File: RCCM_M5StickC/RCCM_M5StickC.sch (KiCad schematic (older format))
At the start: 7 parts, among them CN1 Conn_02x04_Odd_Even, CN2 Conn_01x04, CN3 Conn_01x04, CN4 Conn_01x08

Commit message: Gerber change
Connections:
- net G33: now also S3.6 (Pin_6); no longer S1.6 (Pin_6)
- net SD0: now also S1.6 (Pin_6); no longer S3.6 (Pin_6)
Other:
- moved on the sheet: S1, S3
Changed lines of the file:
@@
 L Conn_01x06 S1
 U 1 1 5EB9082C
-P 1200 1150
-F 0 "S1" H 1200 1450 50  0000 C CNN
-F 1 "Conn_01x06" H 1200 750 50  0000 C CNN
-F 2 "Pin_Headers:Pin_Header_Straight_1x06_Pitch2.54mm" H 1200 1150 50  0001 C CNN
-F 3 "" H 1200 1150 50  0001 C CNN
-	1    1200 1150
+P 2950 1150
+F 0 "S1" H 2950 1450 50  0000 C CNN
+F 1 "Conn_01x06" H 2950 750 50  0000 C CNN
+F 2 "Pin_Headers:Pin_Header_Straight_1x06_Pitch2.54mm" H 2950 1150 50  0001 C CNN
+F 3 "" H 2950 1150 50  0001 C CNN
+	1    2950 1150
 	0    1    -1   0
 $EndComp
@@
 L Conn_01x06 S3
 U 1 1 5EB908B2
-P 2950 1150
-F 0 "S3" H 2950 1450 50  0000 C CNN
-F 1 "Conn_01x06" H 2950 750 50  0000 C CNN
-F 2 "Pin_Headers:Pin_Header_Straight_1x06_Pitch2.54mm" H 2950 1150 50  0001 C CNN
-F 3 "" H 2950 1150 50  0001 C CNN
-	1    2950 1150
+P 1200 1150
+F 0 "S3" H 1200 1450 50  0000 C CNN
+F 1 "Conn_01x06" H 1200 750 50  0000 C CNN
+F 2 "Pin_Headers:Pin_Header_Straight_1x06_Pitch2.54mm" H 1200 1150 50  0001 C CNN
+F 3 "" H 1200 1150 50  0001 C CNN
+	1    1200 1150
 	0    1    -1   0
 $EndComp

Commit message: Gerber Update
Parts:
- added R1, R2: R, Resistors_THT:R_Axial_DIN0207_L6.3mm_D2.5mm_P2.54mm_Vertical, symbol R
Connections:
- net 3V3m: now also R1.1, R2.1
- net G00: now also CN1.8 (Pin_8), CN3.3 (Pin_3), S1.4 (Pin_4), S2.4 (Pin_4), S3.4 (Pin_4), R1.2; no longer CN1.6 (Pin_6), CN3.4 (Pin_4), S1.3 (Pin_3), S2.3 (Pin_3), S3.3 (Pin_3)
- net G26: now also CN1.6 (Pin_6), CN3.4 (Pin_4), S1.3 (Pin_3), S2.3 (Pin_3), S3.3 (Pin_3), R2.2; no longer CN1.8 (Pin_8), CN3.3 (Pin_3), S1.4 (Pin_4), S2.4 (Pin_4), S3.4 (Pin_4)
- net G33: now also S1.6 (Pin_6); no longer S3.6 (Pin_6)
- net SD0: now also S3.6 (Pin_6); no longer S1.6 (Pin_6)
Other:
- moved on the sheet: S1, S3
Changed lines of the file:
@@
 L Conn_01x06 S1
 U 1 1 5EB9082C
-P 2950 1150
-F 0 "S1" H 2950 1450 50  0000 C CNN
-F 1 "Conn_01x06" H 2950 750 50  0000 C CNN
-F 2 "Pin_Headers:Pin_Header_Straight_1x06_Pitch2.54mm" H 2950 1150 50  0001 C CNN
-F 3 "" H 2950 1150 50  0001 C CNN
-	1    2950 1150
+P 1200 1150
+F 0 "S1" H 1200 1450 50  0000 C CNN
+F 1 "Conn_01x06" H 1200 750 50  0000 C CNN
+F 2 "Pin_Headers:Pin_Header_Straight_1x06_Pitch2.54mm" H 1200 1150 50  0001 C CNN
+F 3 "" H 1200 1150 50  0001 C CNN
+	1    1200 1150
 	0    1    -1   0
 $EndComp
@@
 L Conn_01x06 S3
 U 1 1 5EB908B2
-P 1200 1150
-F 0 "S3" H 1200 1450 50  0000 C CNN
-F 1 "Conn_01x06" H 1200 750 50  0000 C CNN
-F 2 "Pin_Headers:Pin_Header_Straight_1x06_Pitch2.54mm" H 1200 1150 50  0001 C CNN
-F 3 "" H 1200 1150 50  0001 C CNN
-	1    1200 1150
+P 2950 1150
+F 0 "S3" H 2950 1450 50  0000 C CNN
+F 1 "Conn_01x06" H 2950 750 50  0000 C CNN
+F 2 "Pin_Headers:Pin_Header_Straight_1x06_Pitch2.54mm" H 2950 1150 50  0001 C CNN
+F 3 "" H 2950 1150 50  0001 C CNN
+	1    2950 1150
 	0    1    -1   0
 $EndComp
@@
 Text Notes 700  850  0    118  ~ 0
 Sensor
-Text GLabel 4900 2050 2    60   Input ~ 0
-G26
-Text GLabel 4900 2150 2    60   Input ~ 0
-G00
 Text GLabel 4650 3850 2    60   Input ~ 0
 G32
@@
 Text GLabel 4450 3950 0    60   Input ~ 0
 SD2
+Text GLabel 4650 3600 2    60   Input ~ 0
+G26
 Text GLabel 4650 3500 2    60   Input ~ 0
-G26
-Text GLabel 4650 3600 2    60   Input ~ 0
 G00
 Text GLabel 4450 3350 0    60   Input ~ 0
@@
 	1100 1800 1100 1350
 Connection ~ 2000 1800
+$Comp
+L R R1
+U 1 1 5EC75A3F
+P 5200 2650
+F 0 "R1" V 5280 2650 50  0000 C CNN
+F 1 "R" V 5200 2650 50  0000 C CNN
+F 2 "Resistors_THT:R_Axial_DIN0207_L6.3mm_D2.5mm_P2.54mm_Vertical" V 5130 2650 50  0001 C CNN
+F 3 "" H 5200 2650 50  0001 C CNN
+	1    5200 2650
+	1    0    0    -1
+$EndComp
+Text GLabel 4900 2050 2    60   Input ~ 0
+SDA
+Text GLabel 4900 2150 2    60   Input ~ 0
+SCL
+Text GLabel 4650 2450 0    60   Input ~ 0
+3V3m
+Text GLabel 4650 2850 0    60   Input ~ 0
+SDA
+Text GLabel 4650 2950 0    60   Input ~ 0
+SCL
+Wire Wire Line
+	4650 2450 5400 2450
+Wire Wire Line
+	5200 2450 5200 2500
+Wire Wire Line
+	4650 2850 5200 2850
+Wire Wire Line
+	5200 2850 5200 2800
+$Comp
+L R R2
+U 1 1 5EC75CCF
+P 5400 2650
+F 0 "R2" V 5480 2650 50  0000 C CNN
+F 1 "R" V 5400 2650 50  0000 C CNN
+F 2 "Resistors_THT:R_Axial_DIN0207_L6.3mm_D2.5mm_P2.54mm_Vertical" V 5330 2650 50  0001 C CNN
+F 3 "" H 5400 2650 50  0001 C CNN
+	1    5400 2650
+	1    0    0    -1
+$EndComp
+Wire Wire Line
+	5400 2450 5400 2500
+Connection ~ 5200 2450
+Wire Wire Line
+	5400 2800 5400 2950
+Wire Wire Line
+	5400 2950 4650 2950
 $EndSCHEMATC

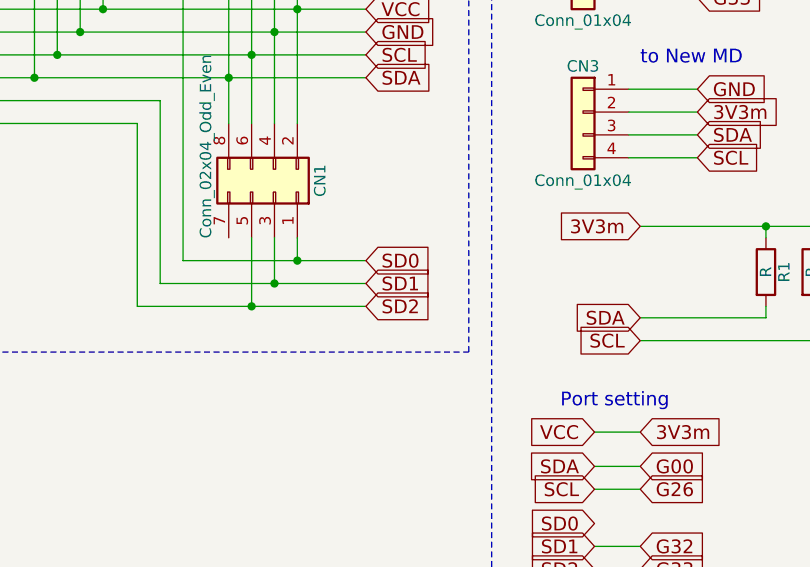
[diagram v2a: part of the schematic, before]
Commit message: SDx Update
(No:Pos:SDx:CNx:Nano:ESP32:M5S),
(S1:LEFT:SD0:CN1-5:No14:IO19:NC),
(S2:CEN:SD1:CN1-3:No15:IO18:G32),
(S3:RIGHT:SD2:CN1-1:No16:IO5:G33)
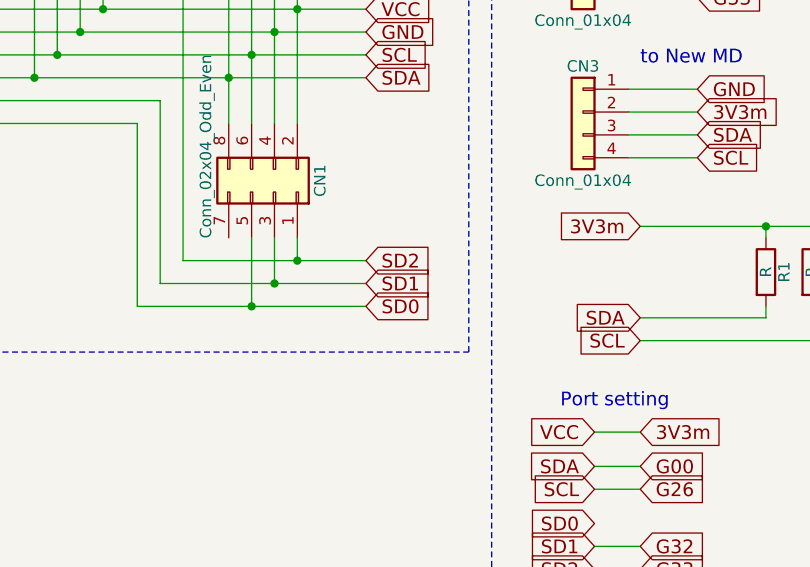
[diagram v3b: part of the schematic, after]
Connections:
- net G33: now also CN1.1 (Pin_1), S3.6 (Pin_6); no longer CN1.5 (Pin_5), S1.6 (Pin_6)
- net SD0: now also CN1.5 (Pin_5), S1.6 (Pin_6); no longer CN1.1 (Pin_1), S3.6 (Pin_6)
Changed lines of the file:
@@
 Text GLabel 3450 1700 2    60   Input ~ 0
 SCL
-Text GLabel 3450 2600 2    60   Input ~ 0
+Text GLabel 3450 2800 2    60   Input ~ 0
 SD0
 Text GLabel 3450 2700 2    60   Input ~ 0
 SD1
-Text GLabel 3450 2800 2    60   Input ~ 0
+Text GLabel 3450 2600 2    60   Input ~ 0
 SD2
 $Comp
